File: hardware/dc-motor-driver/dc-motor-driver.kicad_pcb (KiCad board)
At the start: 2 copper layers, 100 x 90 mm, 85 parts, among them J1 DE9, J10 MOT, J12 MOT, J14 MOT, J2 VIN, J4 MOT, J5 MAG, J6 MOT, J8 MOT, U1 DRV8874PWPR, U2 DRV8874PWPR, U3 DRV8874PWPR, U4 DRV8874PWPR, U5 DRV8874PWPR, U6 DRV8874PWPR, U7 BV1HB045EFJ-CE2

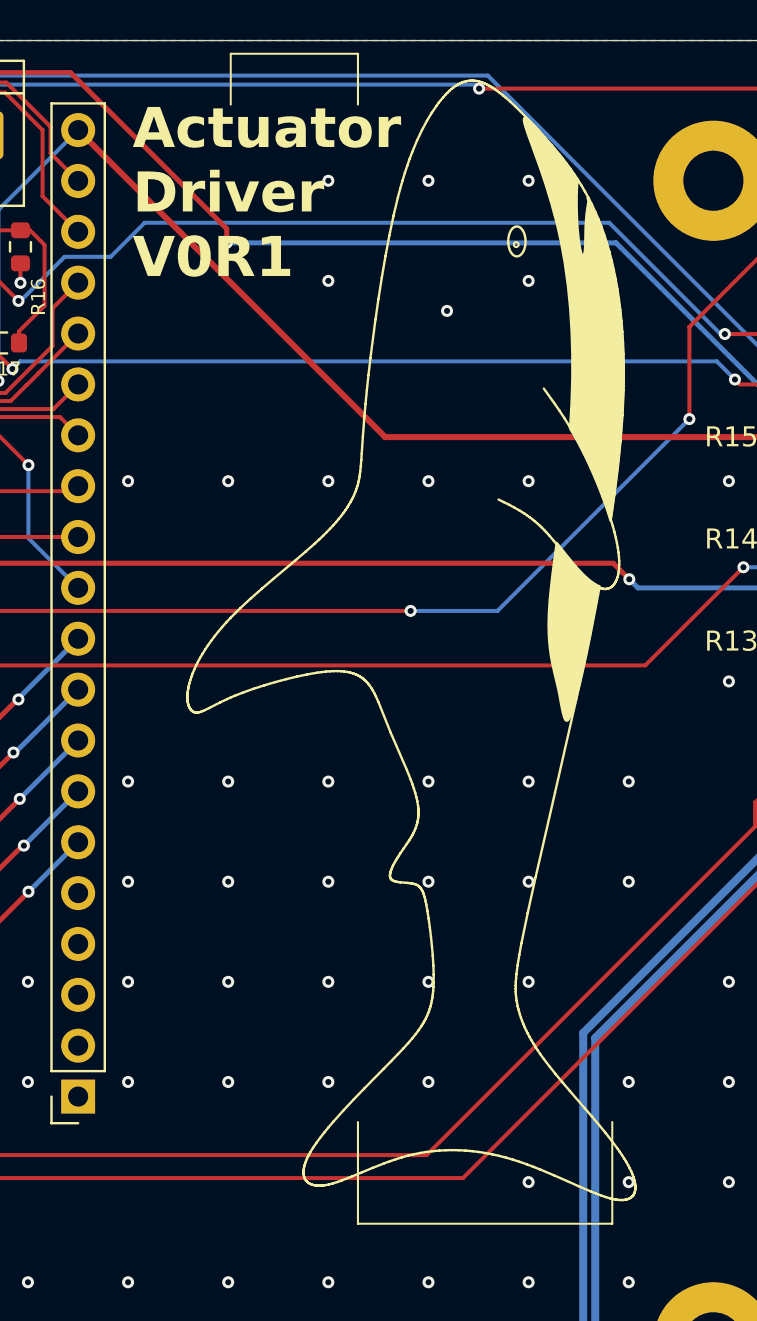
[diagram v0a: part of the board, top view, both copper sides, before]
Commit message: feat: Add Grey silkscreen
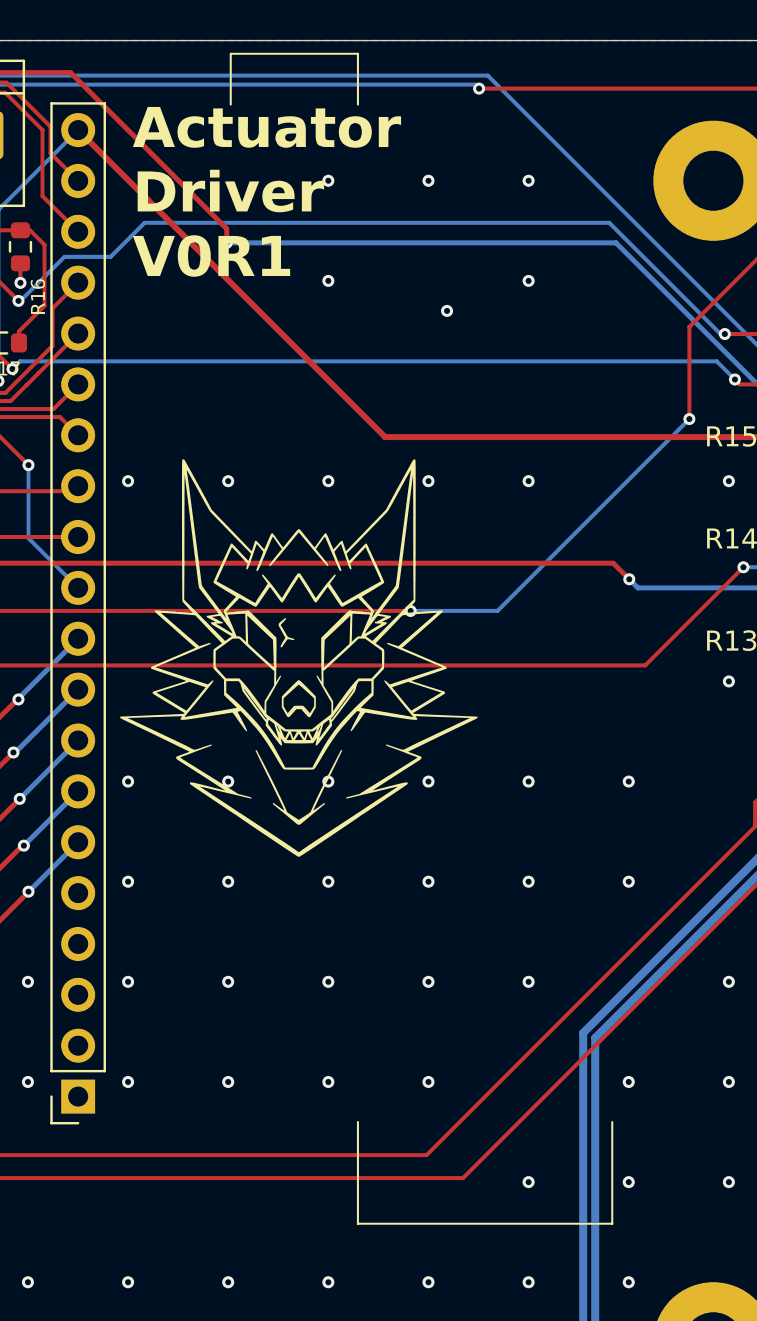
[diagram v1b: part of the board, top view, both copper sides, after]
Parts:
- removed REF**: Smolhaj_Scale_0.1, Symbol:Smolhaj_Scale_0.1
- added G***: LOGO, LOGO, F.Cu at (167.3, 81.9)

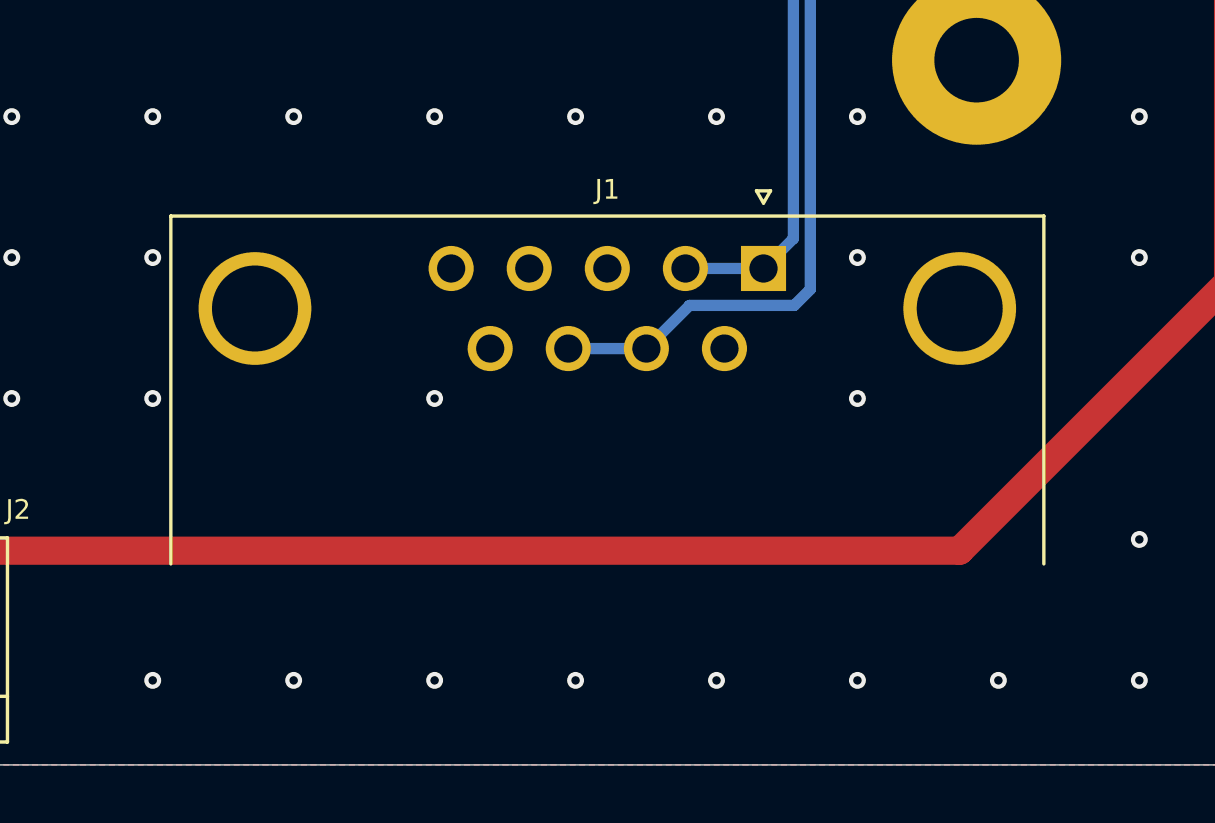
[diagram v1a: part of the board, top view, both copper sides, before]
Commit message: Removed EOL mosfet
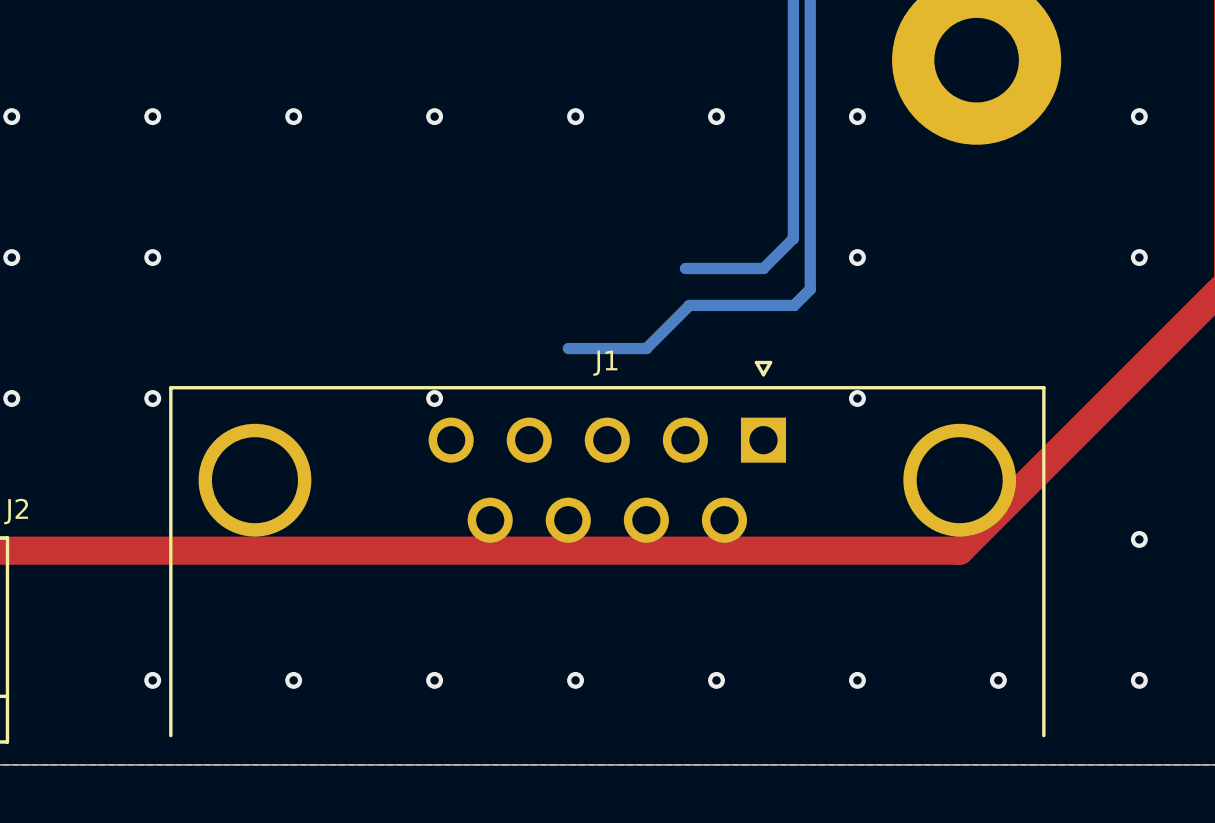
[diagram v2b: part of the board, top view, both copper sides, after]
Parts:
- moved J1 6.09 mm to (180.4, 128.5)
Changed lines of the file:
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@@
 	(footprint "THT:A-DF_09_A_KG-T2S"
 		(layer "F.Cu")
-		(at 180.44 122.389669)
+		(at 180.44 128.48)
 		(descr "9-pin D-Sub connector, horizontal/angled (90 deg), THT-mount, socket (female), pitch 2.77x2.84mm, pin-PCB-offset 7.7mm, distance of mounting holes 25mm, distance of mounting holes to PCB edge 9.12mm, see https://disti-assets.s3.amazonaws.com/tonar/files/datasheets/16730.pdf")
 		(tags "9-pin D-Sub connector horizontal angled 90deg THT socket pitch 2.77x2.84mm pin-PCB-offset 7.7mm mounting-holes-distance 25mm mounting-hole-offset 9.12mm")

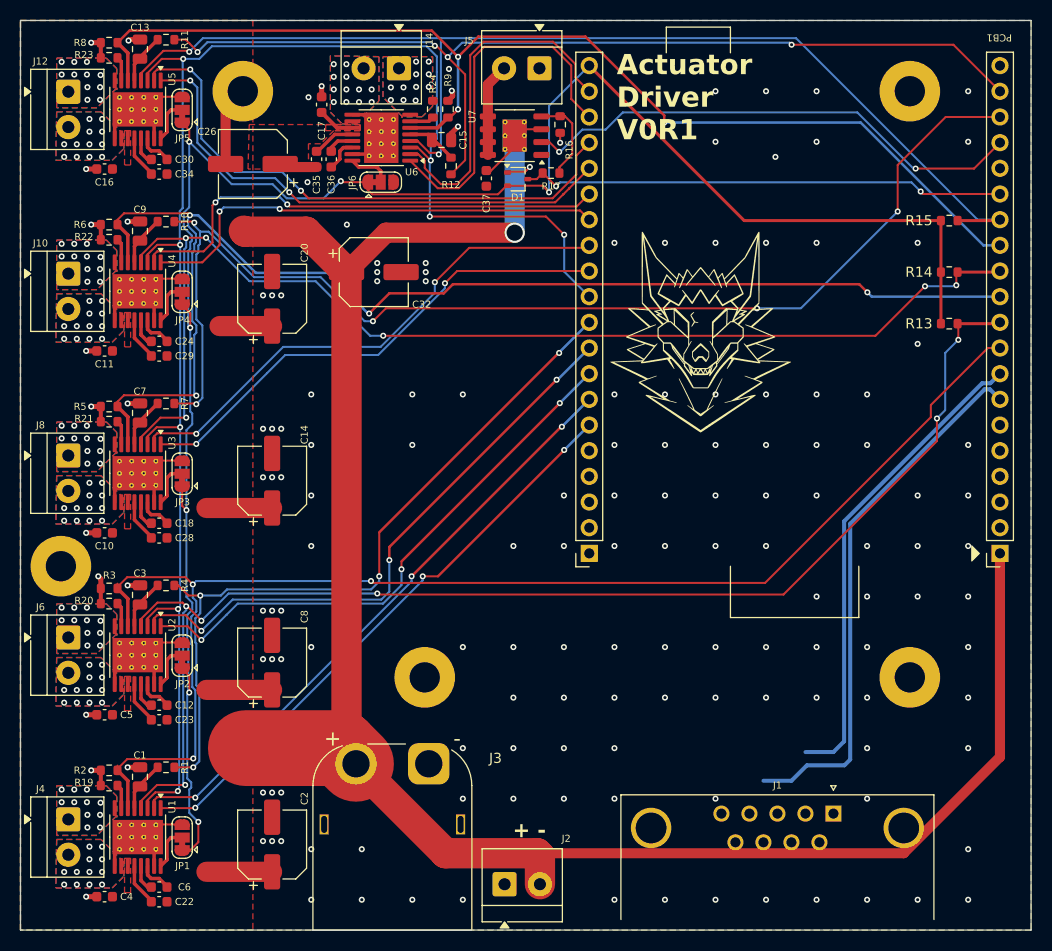
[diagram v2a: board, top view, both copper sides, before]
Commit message: Added new mosfet and silkscreen, DRC and ERC passing
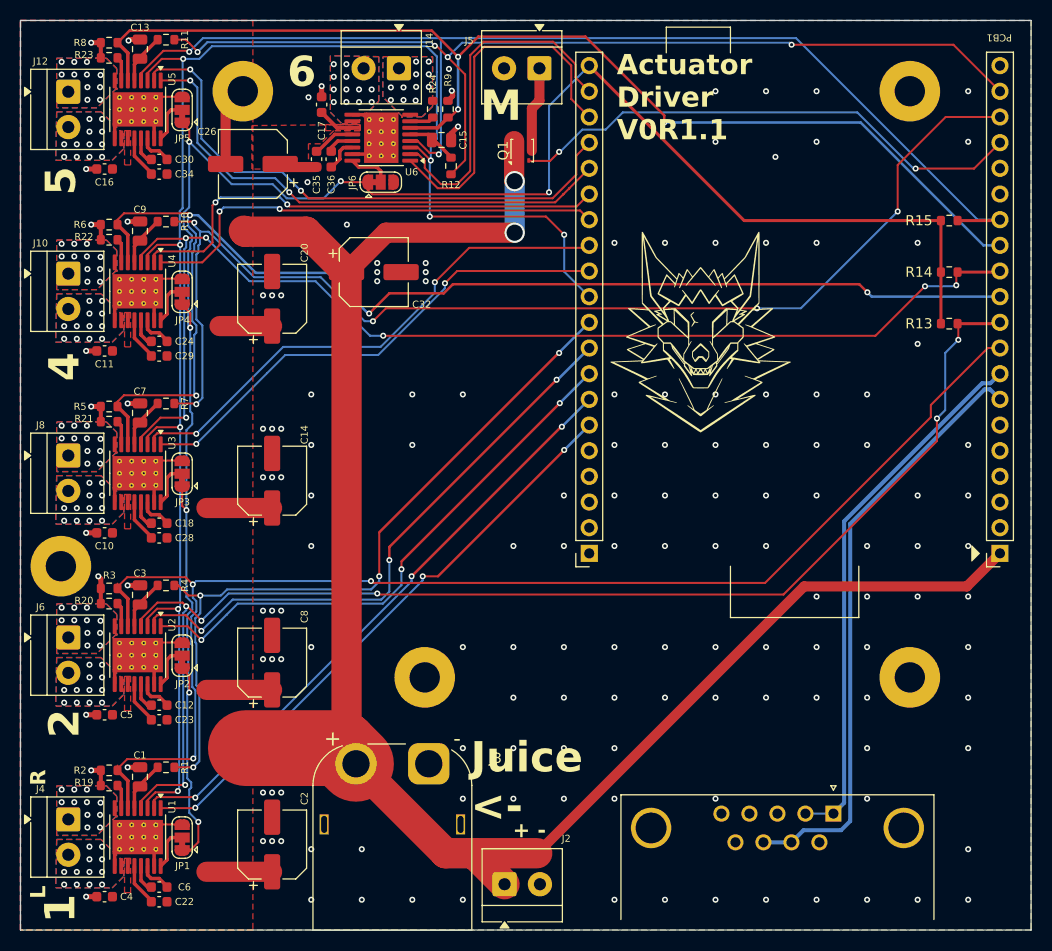
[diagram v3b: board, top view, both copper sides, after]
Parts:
- removed C37: 100n, Capacitor_SMD:C_0603_1608Metric
- removed D1: BAT54SWF, Package_TO_SOT_SMD:SOT-323_SC-70
- removed R16: 1k, Resistor_SMD:R_0603_1608Metric
- removed R17: 10k, Resistor_SMD:R_0603_1608Metric
- removed U7: BV1HB045EFJ-CE2, Package_SO:HTSOP-8-1EP_3.9x4.9mm_P1.27mm_EP2.4x3.2mm_ThermalVias
- added Q1: CSD16301Q2, Package_SON:Texas_DQK, F.Cu at (149.7, 62.9)
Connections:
- J2 pad 1: GND -> VCC
- J2 pad 2: VCC -> GND
- J5 pad 1: GND -> Net-(J5-Pin_1)
- J5 pad 2: Net-(J5-Pin_2) -> GND
- PCB1 pad 15: /MAGNET_I_SENSE -> unconnected-(PCB1-A7-Pad15)
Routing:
- net /MAGNET_I_SENSE: track 48.2 -> 0.00 mm, vias 2 -> 0
- net VCC: track 235.4 -> 216.7 mm, vias 1 -> 2
- net Net-(J5-Pin_2): track 9.24 -> 0.00 mm
- net Net-(U7-SENSE): track 8.79 -> 0.00 mm
- net Net-(J5-Pin_1): track 0.00 -> 8.48 mm
- net /CAN-: track 47.5 -> 53.6 mm
- net /CAN+: track 53.5 -> 59.6 mm
- net GND: track 73.9 -> 70.5 mm, vias 154 -> 152
- net /MAGNET_CTL: track 50.7 -> 52.0 mm
- net +3V3: track 189.6 -> 189.0 mm
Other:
- board text added: "1"
- board text added: "2"
- board text added: "4"
- board text added: "5"
- board text added: "6"
- board text added: "Actuator Driver V0R1.1"
- board text added: "Juice <-"
- board text added: "L"
- board text added: "M"
- board text added: "R"
- board text removed: "Actuator Driver V0R1"
